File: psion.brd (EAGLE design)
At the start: 161.7 x 81.5 mm, 92 parts, among them J2 1-2295018-2, Q1 NTF3055L108T1G, Q2 MMBT2907ALT1G, Q3 NTF3055L108T1G, Q5 MOSFET-PCH_SOT-223, Q6 MOSFET-PCH_SOT-223, T1 2908-05WB-MG, U2 HV823LG-G, U3 ATMEGA32U4-AU, U4 OSD3358-512M-BCB, U5 MAX1620EEE+, U6 MAX1620EEE+, U7 ATTINY404-SSN, U8 TPS61090RSAR, Y1 ABM10-16.000MHZ-D30-T3

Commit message: work on lcd bias power + pdfs
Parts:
- removed C13, C6, C7: 22uf, gothack:CAPCP6032X280N
- removed C3, C4: 0.1uf, dp_devices:C805
- removed C5: 100pf, dp_devices:C805
- removed D2, D3, D6: MBRS0540, ipc-7351-diode:SOD3718X135N
- removed L1: LQH2MCN270K02L, microbuilder:INDUCTOR_1007
- removed Q1: NTF3055L108T1G, SparkFun-DiscreteSemi:SOT23-3
- removed R5: 1M, resistor:R0805
- removed R6: 300k, resistor:R0805
- removed R7: 3.3M, resistor:R0805
- removed R8: 2.2M, resistor:R0805
- added C25, C26: 0.1uf, dp_devices:C805
- added C27, C30: 100pf, dp_devices:C805
- added C28, C29: 22uf, gothack:CAPCP6032X280N
- added D10, D11, D9: MBRS0540, ipc-7351-diode:SOD3718X135N
- added L5: LQH2MCN270K02L, microbuilder:INDUCTOR_1007
- added Q8: MMBT2907ALT1G, ipc-7351-transistor:SOT95P280X135-3N
- added R27: 2.2M, resistor:R0805
- added R28, R30: 10k, resistor:R0805
- added R29: 3.3M, resistor:R0805
- C10: value 22uf -> 100pf; device gothack:CAPCP6032X280N -> dp_devices:C805
- C11: value 1uf -> 22uf; device dp_devices:C805 -> gothack:CAPCP6032X280N
- C12: value 100pf -> 22uf; device dp_devices:C805 -> gothack:CAPCP6032X280N
- Q2: value MMBT2907ALT1G -> NTF3055L108T1G; device ipc-7351-transistor:SOT95P280X135-3N -> SparkFun-DiscreteSemi:SOT23-3
- R10: value 931k -> 300k
- R11: value 300k -> 1M
- R12: value 2.94M -> 300k
- R13: value 10k -> 3.3M
- R14: value 10k -> 2.2M
- R9: value 2.2M -> 1M
- moved C12 21.5 mm to (45.1, 5.84), turned to 270 degrees
- moved C11 20.1 mm to (41.4, 5.84), flipped to the top, turned to 270 degrees
- moved R10 17.2 mm to (29.3, 3.49), turned to 270 degrees
- moved C8 13.6 mm to (39.8, 19.9), turned to 90 degrees
- moved R12 13.6 mm to (42.8, 19.4), turned to 90 degrees
- moved R13 12.8 mm to (46.7, 15.4), flipped to the top, turned to 90 degrees
- moved D4 12.5 mm to (41.9, 15.6), turned to 90 degrees
- moved R11 11.8 mm to (42.8, 15.4), turned to 90 degrees
- moved U5 11.3 mm to (38.9, 14.5), turned to 90 degrees
- moved R14 11.1 mm to (44.8, 11.3), flipped to the top, turned to 270 degrees
- moved Q3 10.7 mm to (38.2, 18.4), turned to 180 degrees
- moved C10 8.61 mm to (44.8, 15.4), turned to 270 degrees
- moved R9 8.58 mm to (29.3, 7.56), turned to 270 degrees
- moved C16 8.52 mm to (50.2, 23.9)
- moved D7 8.52 mm to (50.3, 26.9)
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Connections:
- removed net N$18: Q1.1, U5.15, U5.16
- removed net N$19: D2.A, L1.P$2, Q1.3, U5.14
- removed net N$20: R5.1, U5.10
- removed net N$21: C5.1, R5.2, R6.1, R7.2, U5.9
- removed net N$22: C5.2, C7.P, D2.K, Q2.2, R7.1, R8.1
- removed net N$30: D5.K, R13.1, U5.3
- removed net N$31: C4.1, D5.A, U5.6
- new net N$45: D5.K, R28.1, U5.3
- new net N$46: C9.1, D5.A, U5.6
- new net N$47: R9.1, U6.10
- new net N$48: C27.1, R10.1, R29.2, R9.2, U6.9
- new net N$49: D10.K, R30.1, U6.3
- new net N$50: C26.1, D10.A, U6.6
- new net N$51: C30.2, D11.A, D9.K
- net +3V3: now also C25.1; no longer C3.1
- net GND: now also C11.N, C12.N, C25.2, C26.2, C28.N, C29.P, Q2.2, R10.2, R12.2; no longer C10.N, C13.N, C3.2, C4.2, C6.N, C7.N, Q1.2, R6.2
- net LCD_BIAS_N: now also C27.2, C29.N, D9.A, R29.1; no longer C12.2, C13.P, D3.A, R12.1
- net LCD_BIAS_P: now also Q8.3; no longer Q2.3
- net N$16: now also U5.15, U5.16; no longer U6.15, U6.16
- net N$17: now also D4.A, U5.14; no longer C11.1, U6.14
- net N$23: now also U6.15, U6.16; no longer R8.2, R9.1
- net N$24: now also C30.1, L5.P$2, Q2.3, U6.14; no longer R9.2, U5.8
- net N$25: now also R11.1, U5.10; no longer R10.1, U6.10
- net N$26: now also C10.1, R11.2, R12.1, R13.2, U5.9; no longer C12.1, R10.2, R11.1, R12.2, U6.9
- net N$27: now also C10.2, C12.P, D4.K, Q8.2, R13.1; no longer D6.K, U6.3
- net N$28: now also Q8.1, R14.2, R27.1; no longer C9.1, D6.A, R11.2, U6.6
- net N$32: now also R27.2, U5.8; no longer C11.2, D3.K, D4.A
- net VCCINT: now also C11.P, C28.P, D11.K, L5.P$1, R28.2, R30.2; no longer C10.P, C6.P, D4.K, L1.P$1, R13.2, R14.2
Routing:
- net VCCINT: track 285.8 -> 330.6 mm, vias 8 -> 10
- net GND: track 138.1 -> 160.9 mm, vias 68 -> 70
- net LCD_BIAS_N: track 17.4 -> 37.3 mm, vias 0 -> 3
- net N$22: track 16.8 -> 0.00 mm, vias 1 -> 0
- net N$24: track 2.33 -> 18.5 mm, vias 0 -> 2
- net LCD_BIASP_UP: track 24.7 -> 8.96 mm
- net LCD_BIASP_DN: track 23.6 -> 7.89 mm
- net LCD_EL_EN: track 24.2 -> 8.68 mm
- net N$21: track 12.6 -> 0.00 mm
- net LCD_BIASP_SHDN_: track 26.8 -> 14.4 mm
- net N$26: track 0.32 -> 12.4 mm
- net N$27: track 6.39 -> 17.0 mm
- net N$51: track 0.00 -> 9.27 mm, vias 0 -> 1
- net N$19: track 8.55 -> 0.00 mm, vias 1 -> 0
- net N$48: track 0.00 -> 8.18 mm
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
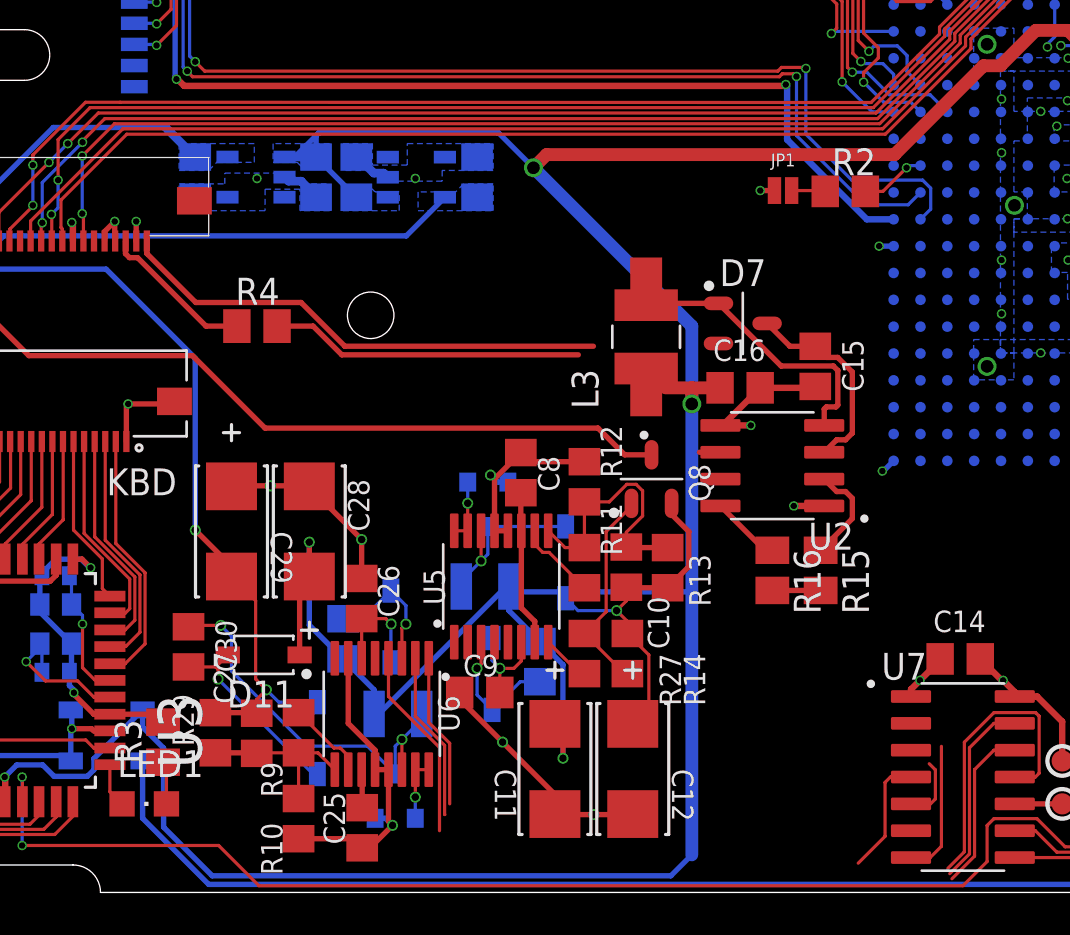
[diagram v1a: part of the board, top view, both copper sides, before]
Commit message: Finally fixed outer dimension polygon + more routing + pdf
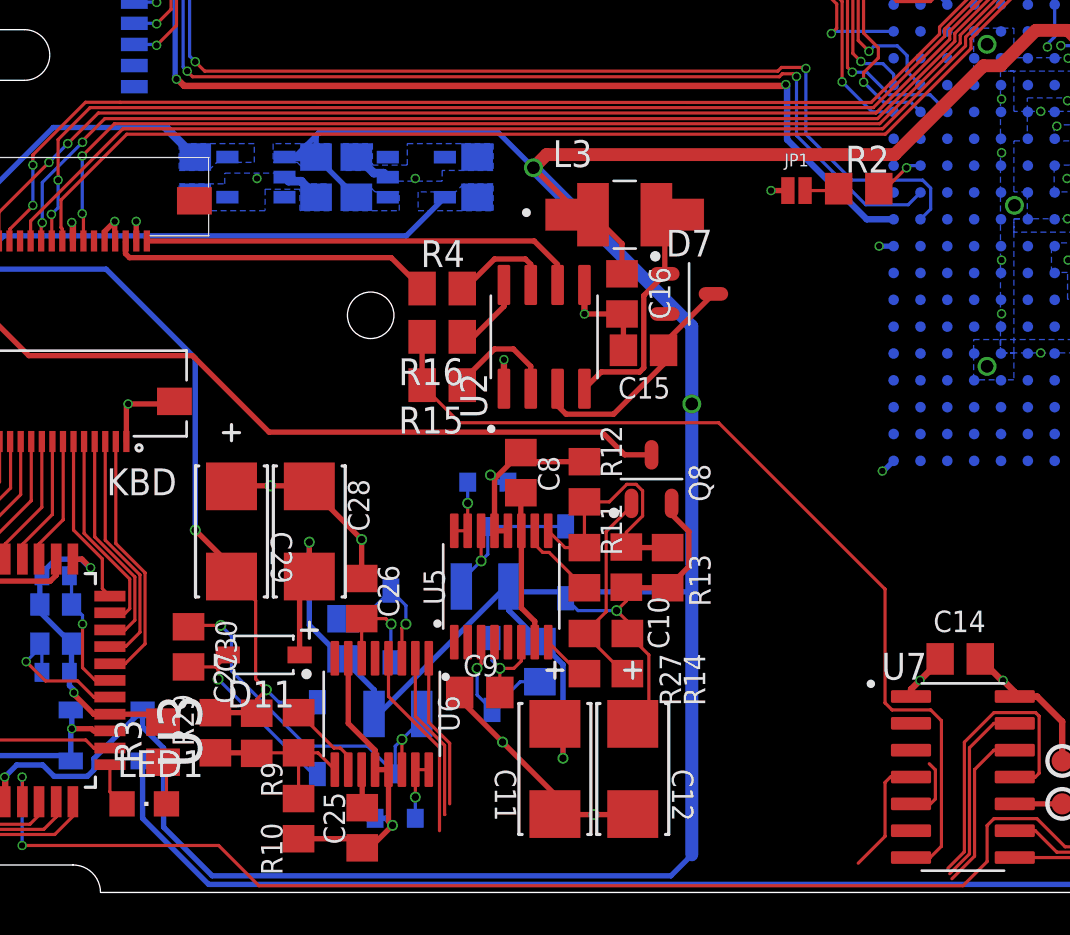
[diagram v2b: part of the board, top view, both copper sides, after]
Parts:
- moved R15 19.9 mm to (36.1, 24.0), turned to 180 degrees
- moved R16 19.1 mm to (36.1, 26.3), turned to 180 degrees
- moved U2 12.4 mm to (40.9, 26.3), turned to 90 degrees
- moved R4 8.94 mm to (36.1, 28.6)
- moved C15 8.16 mm to (45.6, 25.7), turned to 180 degrees
- moved C16 7.14 mm to (44.6, 28.3), turned to 270 degrees
- moved L3 5.87 mm to (44.7, 32.1), turned to 0 degrees
- moved D7 2.90 mm to (47.8, 28.3)
- moved R2 0.65 mm to (55.8, 33.3)
- moved JP1 0.63 mm to (52.8, 33.2)
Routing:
- net LCD_EL_EN: track 8.68 -> 44.2 mm
- net N$15: track 15.7 -> 5.74 mm
- net EL_VA: track 7.30 -> 15.3 mm
- net EL_VB: track 24.5 -> 19.9 mm
- net VCCINT: track 330.6 -> 333.1 mm
- net N$3: track 9.58 -> 12.0 mm
- net GND: track 160.9 -> 159.4 mm
- net N$33: track 4.79 -> 5.73 mm
- net N$1: track 13.6 -> 14.5 mm
- net N$5: track 3.11 -> 2.42 mm

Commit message: routing + gerbers + pdfs + docs
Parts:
- moved TP1 15.7 mm to (50.5, 9.14), turned to 180 degrees
- moved TP2 13.9 mm to (52.2, 2.03), turned to 180 degrees
- moved C14 10.3 mm to (55.4, 2.16), turned to 180 degrees
- moved U7 5.97 mm to (55.2, 7.87), turned to 180 degrees
- moved R17 1.35 mm to (79.6, 13.8), turned to 90 degrees
- moved C10 0.38 mm to (45.2, 15.4)
- moved C11 0.38 mm to (41.8, 5.84)
- moved C12 0.38 mm to (45.5, 5.84)
- moved C8 0.38 mm to (40.2, 19.9)
- moved C9 0.38 mm to (38.2, 9.46)
- moved D4 0.38 mm to (42.3, 15.6)
- moved D5 0.38 mm to (38.8, 10.3)
- moved L2 0.38 mm to (38.5, 14.5)
- moved Q3 0.38 mm to (38.6, 18.4)
- moved Q8 0.38 mm to (46.4, 19.6)
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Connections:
- net N$15 renamed EL_VA_PRE
- net N$17 renamed LCD_BIAS_P_P1
- net N$24 renamed LCD_BIAS_N_P1
- net N$27 renamed LCD_BIAS_P_P2
- net N$36 renamed USBC_IND_SW
- net N$41 renamed USBC_VBUS_SW
- net N$51 renamed LCD_BIAS_N_P2
- net LCD_BIASN_DN: now also U7.3; no longer U7.4
- net LCD_BIASN_SHDN_: now also U7.5; no longer U7.3
- net LCD_BIASN_UP: now also U7.4; no longer U7.5
- net LCD_BIASP_SHDN_: now also U7.13; no longer U7.11
- net LCD_BIASP_UP: now also U7.11; no longer U7.13
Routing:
- net LCD_BIASN_SHDN_: track 9.16 -> 42.9 mm
- net VCCINT: track 333.1 -> 303.1 mm, vias 10 -> 9
- net LCD_BIASN_UP: track 11.0 -> 40.3 mm
- net LCD_BIASN_DN: track 13.0 -> 38.0 mm
- net LCD_BIASP_UP: track 8.96 -> 31.8 mm
- net LCD_BIASP_DN: track 7.89 -> 30.6 mm
- net LCD_BIASP_SHDN_: track 14.4 -> 34.3 mm
- net LCD_EL_EN: track 44.2 -> 33.5 mm
- net I2C0_SDA: track 151.6 -> 159.5 mm
- net N$37: track 1.91 -> 8.55 mm
- net +3V3: track 20.6 -> 24.7 mm, vias 7 -> 10
- net GND: track 159.4 -> 155.6 mm, vias 70 -> 71
- net N$1: track 14.5 -> 11.0 mm
- net I2C0_SCL: track 150.5 -> 153.5 mm
- net N$38: track 80.3 -> 78.2 mm
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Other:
- outline, holes or cut-outs redrawn

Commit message: add TAPR OHL license
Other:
- board text added: "PsiOnSD (c)Greg "GothAck" Miell 2019 Licensed under the TAPR OHL (www.tapr.org/OHL)"
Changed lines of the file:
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@@
 <circle x="30.099" y="66.167" radius="0.225" width="0" layer="199"/>
 <circle x="23.4454" y="65.1014" radius="0.15" width="0" layer="199"/>
+<text x="61.087" y="0.889" size="1.016" layer="25" font="vector">PsiOnSD
+(c)Greg "GothAck" Miell 2019
+Licensed under the TAPR OHL (www.tapr.org/OHL)</text>
 </plain>
 <attributes>
@@
 </drawing>
 <compatibility>
+<note version="6.3" minversion="6.2.2" severity="warning">
+Since Version 6.2.2 text objects can contain more than one line,
+which will not be processed correctly with this version.
+</note>
 <note version="8.2" severity="warning">
 Since Version 8.2, EAGLE supports online libraries. The ids

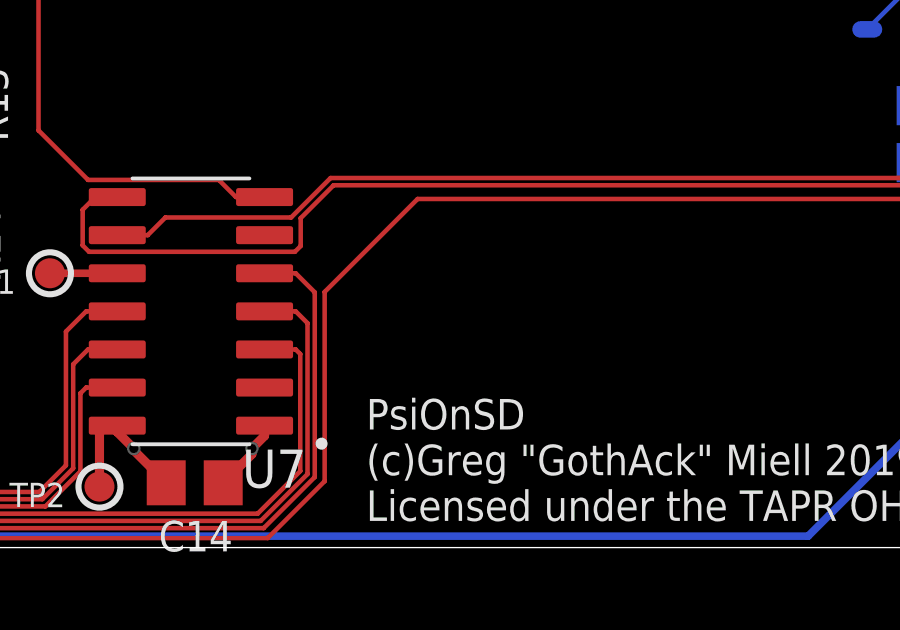
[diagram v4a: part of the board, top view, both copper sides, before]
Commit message: Add OSHW to brd
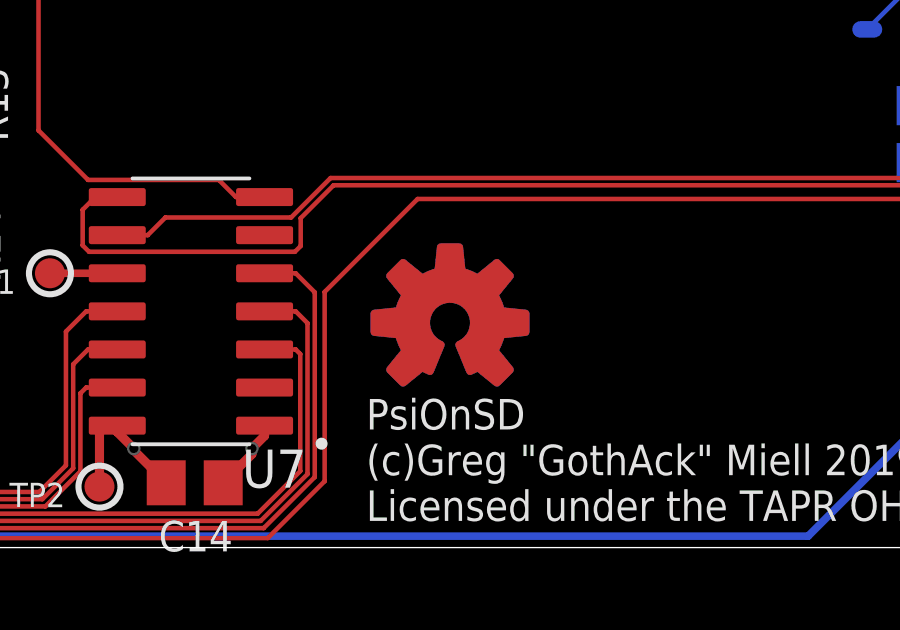
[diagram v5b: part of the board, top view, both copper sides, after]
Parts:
- added U$5, U$7: (no value), adafruit:OSHWLOGO_TOP_0.2
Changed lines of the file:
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@@
 <board_group name="KBD_USB"/>
 <board_group name="EL_BACKLIGHT"/>
+<board_group name="OSHW_LOGO"/>
 </groups>
 <elements>
@@
 <attribute name="VALUE" x="21.844" y="12.8905" size="1.016" layer="27" ratio="12" rot="R270"/>
 </element>
+<element name="U$5" library="adafruit" library_urn="urn:adsk.eagle:library:420" package="OSHWLOGO_TOP_0.2" value="" x="63.881" y="7.493" smashed="yes" grouprefs="OSHW_LOGO"/>
+<element name="U$7" library="adafruit" library_urn="urn:adsk.eagle:library:420" package="OSHWLOGO_TOP_0.2" value="" x="63.881" y="7.493" smashed="yes" rot="MR0" grouprefs="OSHW_LOGO"/>
 </elements>
 <signals>
